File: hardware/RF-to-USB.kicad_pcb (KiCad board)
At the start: 4 copper layers, 50 x 20 mm, 53 parts, among them J1 USB_A, J2 SMA-F, J3 ARM SWD, SW1 BTN1, SW2 BTN2, U1 nRF24L01P, U2 STM32L432KBUx, U3 XC6206P332MR, U4 USBLC6-2SC6, U5 OLED Display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

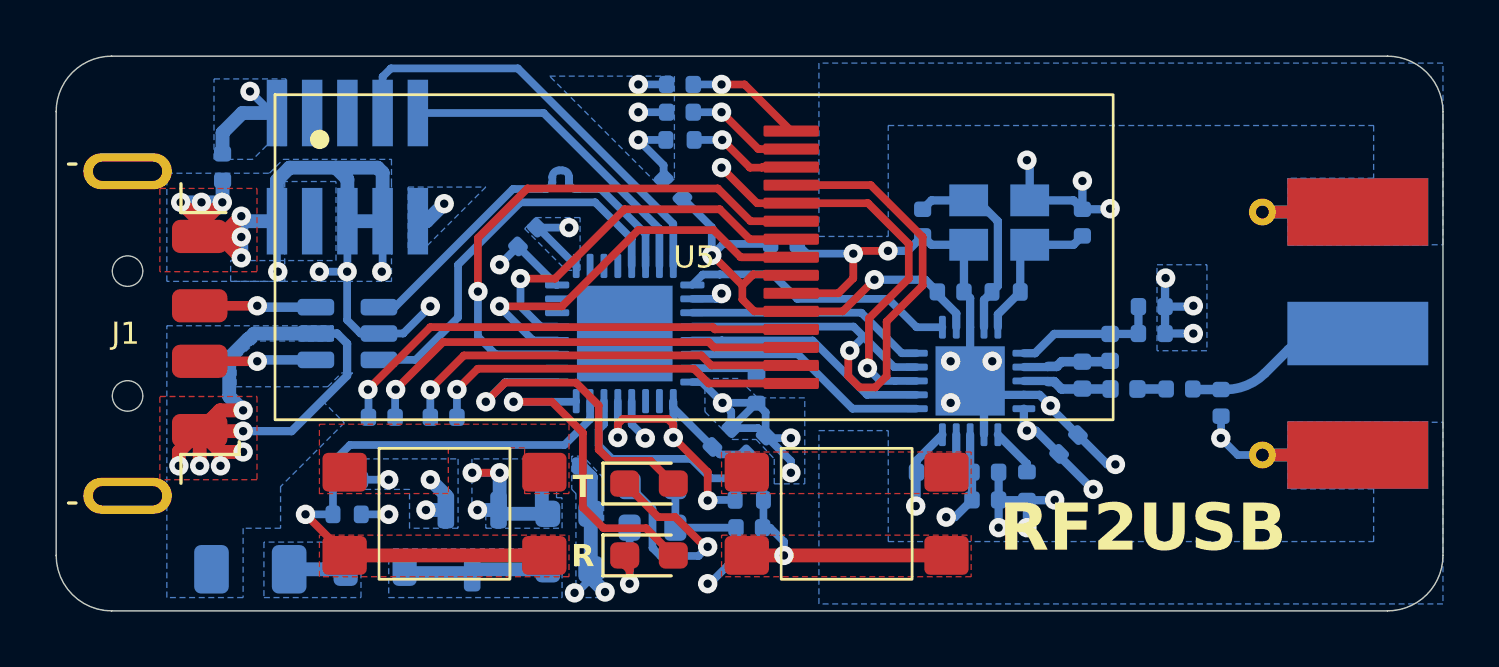
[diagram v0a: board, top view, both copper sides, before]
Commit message: silkscreen adjustments
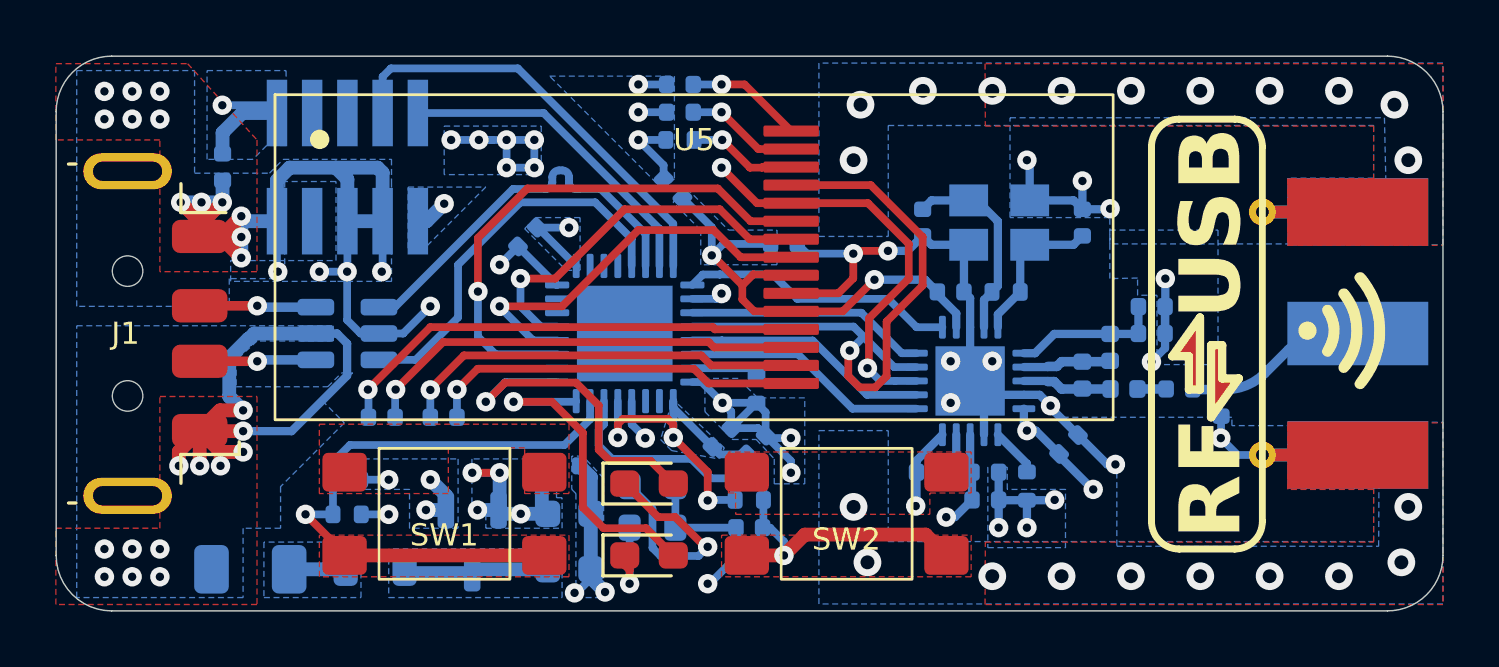
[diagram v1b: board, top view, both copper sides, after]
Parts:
- added G***: LOGO, LOGO, F.Cu at (122.0, 48.5)
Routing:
- net GND: track 117.7 -> 124.9 mm, vias 42 -> 74
- net BTN2_EXTI: track 18.4 -> 19.0 mm
- net +3V3: track 52.2 -> 52.4 mm, vias 14 -> 15
- net +5V: vias 6 -> 12
- added copper zone on In1.Cu, net +3V3
- added copper zone on In2.Cu, net GND
- removed copper zone on In2.Cu, net +3V3
- removed copper zone on In1.Cu, net GND
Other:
- board text added: "RF"
- board text added: "USB"
- board text removed: "R"
- board text removed: "RF2USB"
- board text removed: "T"
